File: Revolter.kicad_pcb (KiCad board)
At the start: 2 copper layers, 100 x 100 mm, 183 parts, among them IC1 LM5017, IC2 AP65111, IC3 INA181A1, IC4 INA181A1, J1 IO, P1 USB_OTG, P2 CAN, P3 IN+, P4 IN-, P5 MOTOR3, P6 MOTOR2, P7 MOTOR1, P8 SWD, P9 Motor, Q1 ZXTC2045E6, Q10 ZXTC2045E6, Q13 IRFB4110, Q14 IRFB4110, Q15 IRFB4110, Q16 IRFB4110, Q19 IRFB4110, Q2 ZXTC2045E6, Q20 IRFB4110, Q21 IRFB4110, Q22 IRFB4110, Q3 IRFB4110, Q4 IRFB4110, Q5 ZXTC2045E6, Q6 ZXTC2045E6, Q7 IRFB4110, Q8 IRFB4110, Q9 ZXTC2045E6, U1 STM32F40X_LQFP64, U2 IR2110S, U3 IR2110S, U4 IR2110S, U5 PCA82C251, U6 7805_SO8, Y1 Crystal

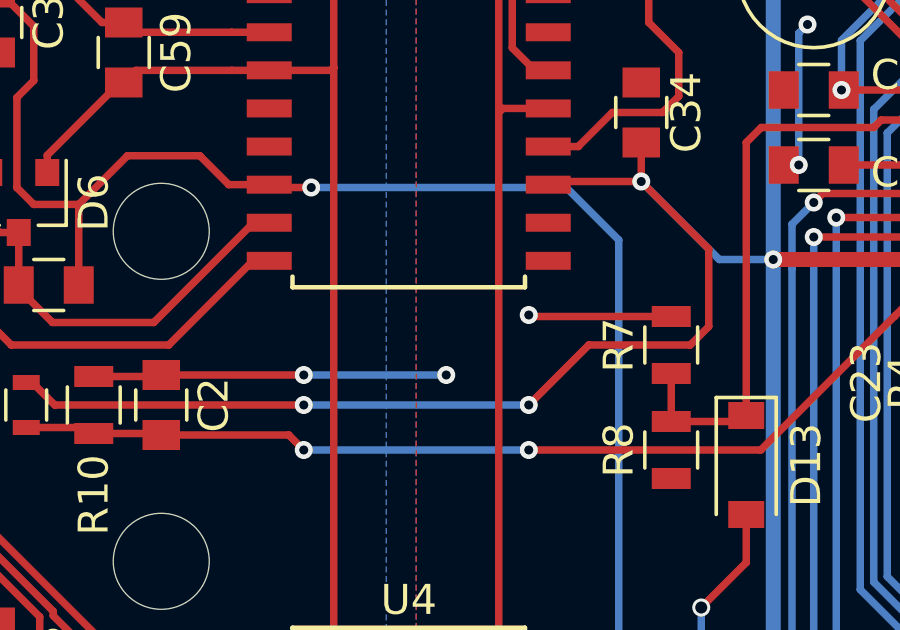
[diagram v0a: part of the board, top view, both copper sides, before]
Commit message: - fixed V_IN ADC channel missing a trace
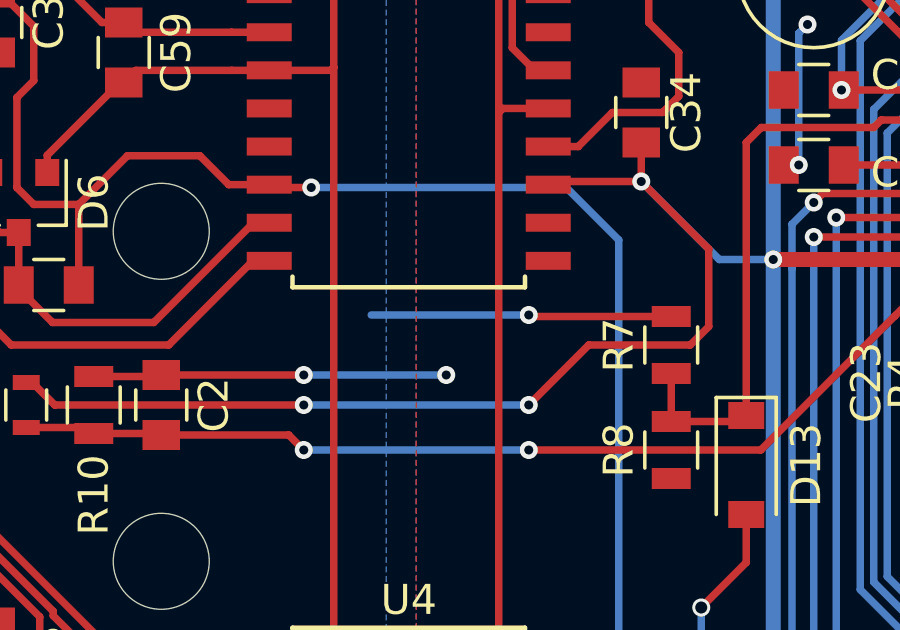
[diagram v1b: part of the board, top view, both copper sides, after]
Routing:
- net +BATT: track 46.9 -> 52.1 mm
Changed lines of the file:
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@@
     (thickness 1.6)
     (drawings 12)
-    (tracks 1598)
+    (tracks 1599)
     (zones 0)
     (modules 183)
@@
   (segment (start 110.525 132.7775) (end 110.2525 133.05) (width 0.5) (layer F.Cu) (net 32))
   (segment (start 110.2525 133.05) (end 108.75 133.05) (width 0.5) (layer F.Cu) (net 32))
+  (segment (start 118.25 66.25) (end 113 66.25) (width 0.25) (layer B.Cu) (net 32))
   (segment (start 134.25 69.45) (end 134.25 72.15) (width 0.25) (layer F.Cu) (net 33))
   (segment (start 137.35 72.15) (end 138.25 71.25) (width 0.25) (layer F.Cu) (net 34))

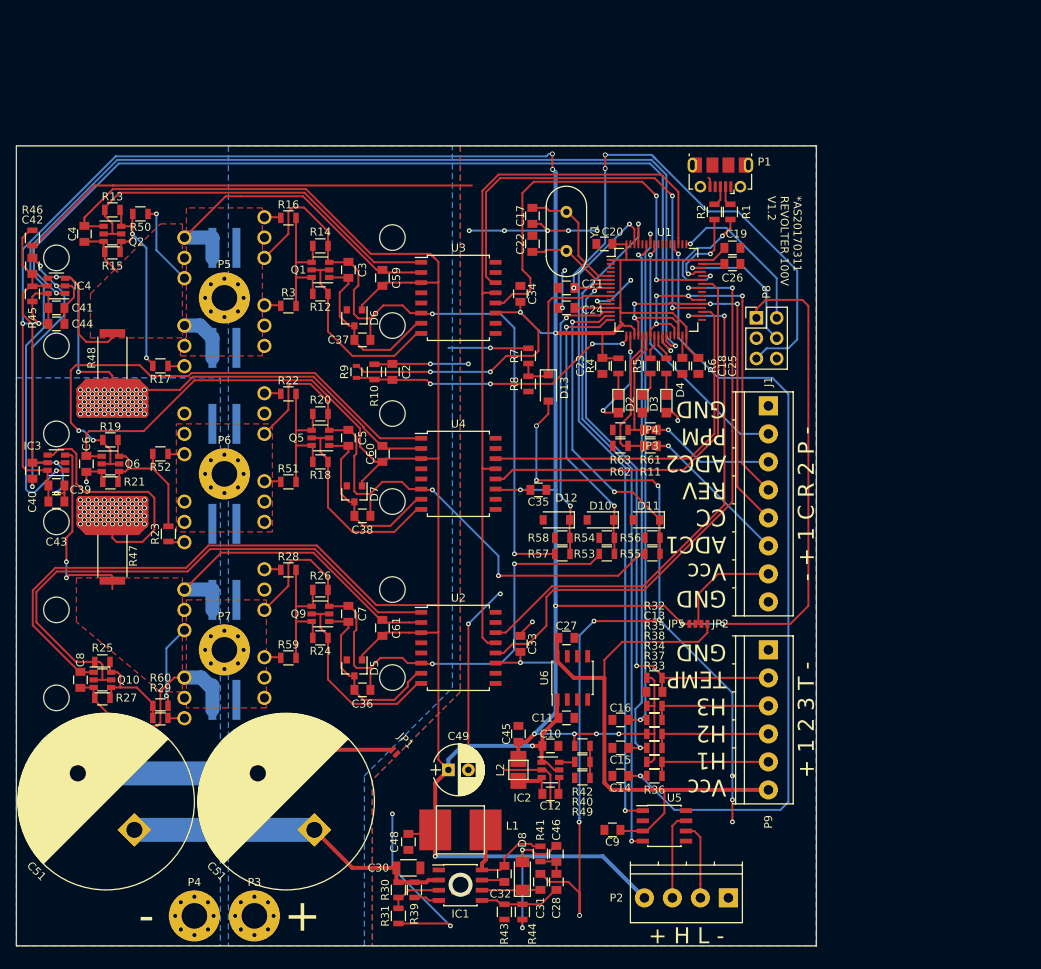
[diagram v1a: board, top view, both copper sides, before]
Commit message: - swapped TO220 dual MOSFET for single DualCool88 MOSFET package - removed postdriver - changed IRS2110 for IRS2186 - added third shunt - rewired CPU for VESC6 compatibility - layout completely from scratch
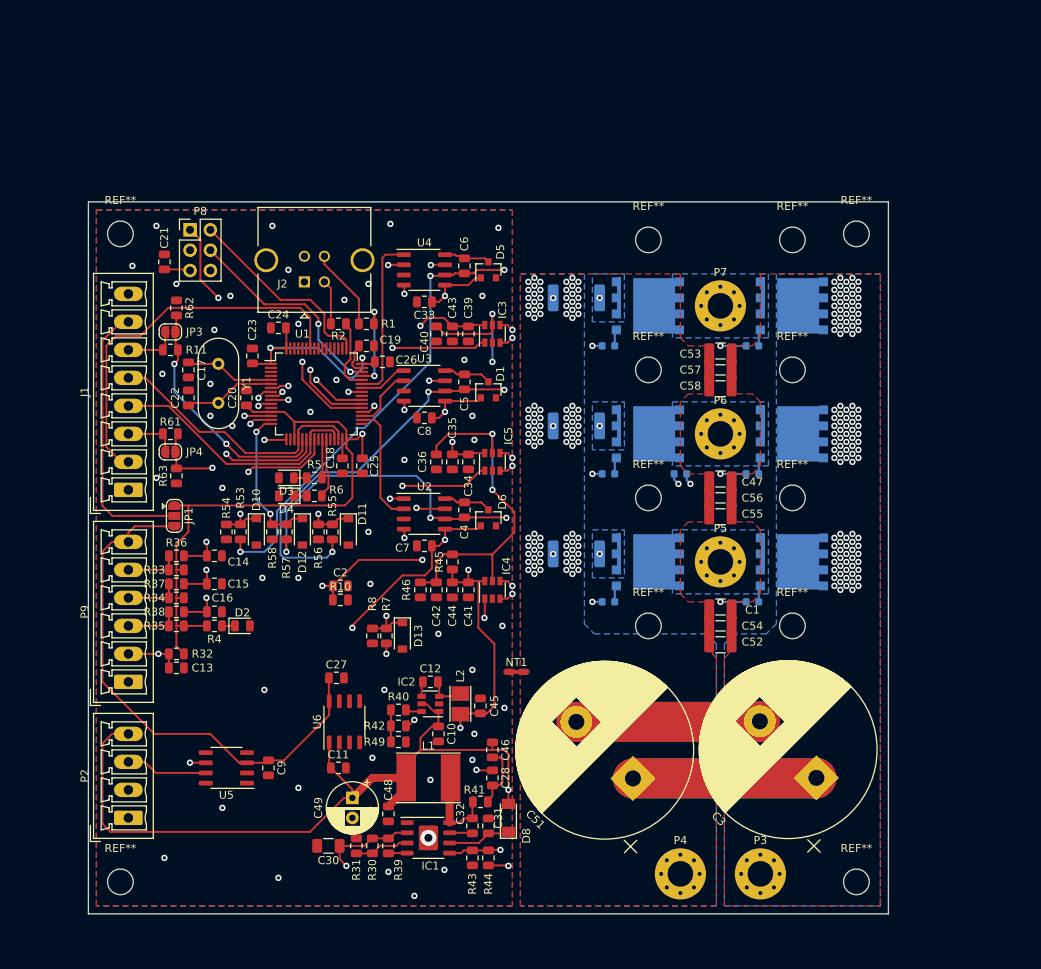
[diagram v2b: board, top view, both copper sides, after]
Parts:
- removed C29, C50, C62: 2u2 250V, Capacitors_SMD:C_1210
- removed C37, C38, C59, C60, C61: 100n, Capacitors_SMD:C_0805
- removed the C51 at (73.8, 126.5)
- removed the C51 at (96.2, 126.5)
- removed D7: BAS21L, Diodes_SMD:D_SOT-23_ANK
- removed JP2, JP5: opt., alexmod:Jumper_2
- removed P1: USB_OTG, Connectors_USB:USB_Micro-B_Molex-105017-0001
- removed Q10, Q9: ZXTC2045E6, TO_SOT_Packages_SMD:SOT-23-6
- removed Q13, Q14, Q15, Q16, Q19, Q20, Q21, Q22, Q7, Q8: IRFB4110, alexmod:TO220GDS_notab_rev
- removed R12, R13, R18, R19, R24, R25: 120R, Resistors_SMD:R_0805
- removed R14, R15, R20, R21, R26, R27: 10k, Resistors_SMD:R_0805
- removed R50, R51, R52, R59, R60: 1R, Resistors_SMD:R_0805
- added C51: 1mF 100V, Capacitor_THT:CP_Radial_D22.0mm_P10.00mm_SnapIn, F.Cu at (136.1, 120.1)
- added D1: BAS21L, Diode_SMD:D_SOT-23_ANK, F.Cu at (118.0, 71.5)
- added IC5: INA181A1, Package_TO_SOT_SMD:SOT-23-6, F.Cu at (118.5, 80.5)
- added J2: USB_A, Connector_USB:USB_B_TE_5787834_Vertical, F.Cu at (95.0, 58.0)
- added NT1: Net-Tie_2, NetTie:NetTie-2_SMD_Pad0.5mm, F.Cu at (121.5, 106.8)
- added REF**: MountingHole_3.2mm_M3, MountingHole:MountingHole_3.2mm_M3, F.Cu at (156.0, 52.8)
- added REF**: MountingHole_3.2mm_M3, MountingHole:MountingHole_3.2mm_M3, F.Cu at (138.0, 85.0)
- added REF**: MountingHole_3.2mm_M3, MountingHole:MountingHole_3.2mm_M3, F.Cu at (138.0, 69.0)
- added REF**: MountingHole_3.2mm_M3, MountingHole:MountingHole_3.2mm_M3, F.Cu at (138.0, 52.8)
- added REF**: MountingHole_3.2mm_M3, MountingHole:MountingHole_3.2mm_M3, F.Cu at (156.0, 69.0)
- added REF**: MountingHole_3.2mm_M3, MountingHole:MountingHole_3.2mm_M3, F.Cu at (156.0, 85.0)
- added REF**: MountingHole_3.2mm_M3, MountingHole:MountingHole_3.2mm_M3, F.Cu at (156.0, 101.0)
- added REF**: MountingHole_3.2mm_M3, MountingHole:MountingHole_3.2mm_M3, F.Cu at (164.0, 52.0)
- added REF**: MountingHole_3.2mm_M3, MountingHole:MountingHole_3.2mm_M3, F.Cu at (164.0, 133.0)
- added REF**: MountingHole_3.2mm_M3, MountingHole:MountingHole_3.2mm_M3, F.Cu at (72.0, 133.0)
- added REF**: MountingHole_3.2mm_M3, MountingHole:MountingHole_3.2mm_M3, F.Cu at (72.0, 52.0)
- added REF**: MountingHole_3.2mm_M3, MountingHole:MountingHole_3.2mm_M3, F.Cu at (138.0, 101.0)
- C1, C47, C52, C53, C54, C55, C56, C57, C58: footprint Capacitors_SMD:C_1210 -> Capacitor_SMD:C_1210_3225Metric; moved to F.Cu
- C10, C11, C12, C13, C14, C15, C16, C17, C18, C19, C2, C20, C21, C22, C23, C24, C25, C26, C27, C28, C31, C32, C36, C39, C4, C40, C41, C42, C43, C44, C45, C46, C48, C5, C6, C7, C8, C9: footprint Capacitors_SMD:C_0805 -> Capacitor_SMD:C_0805_2012Metric
- C3: value 1u -> 1mF 100V; footprint Capacitors_SMD:C_0805 -> Capacitor_THT:CP_Radial_D22.0mm_P10.00mm_SnapIn
- C30: footprint Capacitors_SMD:C_1206 -> Capacitor_SMD:C_1206_3216Metric
- C33, C35: value 100n -> 1u; footprint Capacitors_SMD:C_0805 -> Capacitor_SMD:C_0805_2012Metric
- C34: value 100n -> 10n; footprint Capacitors_SMD:C_0805 -> Capacitor_SMD:C_0805_2012Metric
- C49: footprint Capacitors_THT:CP_Radial_D6.3mm_P2.50mm -> Capacitor_THT:CP_Radial_D6.3mm_P2.50mm
- D10, D11, D12, D13: footprint Diodes_SMD:D_SOD-123 -> Diode_SMD:D_SOD-123
- D2, D3, D4: footprint LEDs:LED_0805 -> LED_SMD:LED_0805_2012Metric
- D5, D6: footprint Diodes_SMD:D_SOT-23_ANK -> Diode_SMD:D_SOT-23_ANK
- D8: footprint Diodes_SMD:D_MiniMELF_Standard -> Diode_SMD:D_MiniMELF
- IC1: footprint Housings_SOIC:SOIC-8-1EP_3.9x4.9mm_Pitch1.27mm -> Package_SO:HSOP-8-1EP_3.9x4.9mm_P1.27mm_EP2.41x3.1mm
- IC2, IC3, IC4: footprint TO_SOT_Packages_SMD:SOT-23-6 -> Package_TO_SOT_SMD:SOT-23-6
- J1: footprint Connectors_Terminal_Blocks:TerminalBlock_Pheonix_PT-3.5mm_8pol -> Connector_Phoenix_MC:PhoenixContact_MCV_1,5_8-G-3.5_1x08_P3.50mm_Vertical
- JP1: value JUMPER -> Jumper_NC_Dual; footprint alexmod:Jumper_2 -> Jumper:SolderJumper-3_P1.3mm_Open_RoundedPad1.0x1.5mm
- JP3, JP4: footprint alexmod:Jumper_2 -> Jumper:SolderJumper-2_P1.3mm_Open_RoundedPad1.0x1.5mm
- L1: footprint alexmod:VLS6045EX -> Inductor_SMD:L_Taiyo-Yuden_NR-60xx_HandSoldering
- L2: footprint alexmod:NRH2410 -> Inductor_SMD:L_Taiyo-Yuden_NR-24xx_HandSoldering
- P2: footprint Connectors_Terminal_Blocks:TerminalBlock_Pheonix_PT-3.5mm_4pol -> Connector_Phoenix_MC:PhoenixContact_MCV_1,5_4-G-3.5_1x04_P3.50mm_Vertical
- P3, P4, P5, P6, P7: footprint Mounting_Holes:MountingHole_3.2mm_M3_Pad_Via -> MountingHole:MountingHole_3.2mm_M3_Pad_Via
- P8: footprint Pin_Headers:Pin_Header_Straight_2x03_Pitch2.54mm -> Connector_PinHeader_2.54mm:PinHeader_2x03_P2.54mm_Vertical
- P9: footprint Connectors_Terminal_Blocks:TerminalBlock_Pheonix_PT-3.5mm_6pol -> Connector_Phoenix_MC:PhoenixContact_MCV_1,5_6-G-3.5_1x06_P3.50mm_Vertical
- Q1, Q2, Q5, Q6: value ZXTC2045E6 -> FDMT800100DC; footprint TO_SOT_Packages_SMD:SOT-23-6 -> Package_TO_SOT_SMD:PQFN_8x8; moved to B.Cu
- Q3, Q4: value IRFB4110 -> FDMT800100DC; footprint alexmod:TO220GDS_notab_rev -> Package_TO_SOT_SMD:PQFN_8x8
- R1, R10, R11, R2, R30, R31, R32, R33, R34, R35, R36, R37, R38, R39, R4, R40, R41, R42, R43, R44, R45, R46, R49, R5, R53, R54, R55, R56, R57, R58, R6, R61, R62, R63, R7, R8: footprint Resistors_SMD:R_0805 -> Resistor_SMD:R_0805_2012Metric
- R16, R17, R22, R23, R28, R29: footprint Resistors_SMD:R_0805 -> Resistor_SMD:R_0603_1608Metric; moved to B.Cu
- R3: value 1R -> WSLF2512L5000FEB; footprint Resistors_SMD:R_0805 -> Resistor_SMD:R_2512_6332Metric; moved to B.Cu
- R47, R48: footprint Resistors_SMD:R_2512 -> Resistor_SMD:R_2512_6332Metric; moved to B.Cu
- R9: footprint Resistors_SMD:R_0603 -> Resistor_SMD:R_0603_1608Metric; moved to B.Cu
- U1: footprint Housings_QFP:LQFP-64_10x10mm_Pitch0.5mm -> Package_QFP:LQFP-64_10x10mm_P0.5mm
- U2, U3, U4: value IR2110S -> IRS2186; footprint Housings_SOIC:SOIC-16W_7.5x10.3mm_Pitch1.27mm -> Package_SO:SO-8_3.9x4.9mm_P1.27mm
- U5, U6: footprint Housings_SOIC:SOIC-8_3.9x4.9mm_Pitch1.27mm -> Package_SO:SO-8_3.9x4.9mm_P1.27mm
- Y1: footprint Crystals:Crystal_HC49-U_Vertical -> Crystal:Crystal_HC49-U_Vertical
- moved C3 86.3 mm to (159.0, 120.0), turned to 135 degrees
- moved J1 80.7 mm to (73.0, 84.0), turned to 90 degrees
- moved P9 80.1 mm to (73.0, 108.0), turned to 90 degrees
- moved C54 78.7 mm to (147.0, 101.0)
- moved Q2 78.5 mm to (137.9, 93.0)
- moved P2 75.7 mm to (73.0, 125.0), turned to 90 degrees
- moved P7 75.5 mm to (147.0, 61.0)
- moved R16 75.3 mm to (151.0, 98.0), turned to 180 degrees
- moved C58 74.1 mm to (147.0, 71.0)
- moved R29 72.8 mm to (133.0, 66.0)
- moved P8 71.6 mm to (80.7, 51.5)
- moved C52 71.4 mm to (147.0, 103.0)
- moved C1 70.7 mm to (147.0, 99.0)
- moved Q3 70.4 mm to (155.9, 77.0)
- moved P5 70.2 mm to (147.0, 93.0)
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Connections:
- net /MCU/DC_CAL renamed Net-(U1-Pad33)
- net /MCU/FAULT renamed Net-(U1-Pad53)
- net /MCU/SENS2 renamed /MCU/VOLTAGE_2
- C1 pad 2: /Mosfet driver/H1_LOW -> GNDPWR
- C3 pad 1: /Mosfet driver/H1_HI -> +BATT
- C3 pad 2: /Mosfet driver/H1_VS -> GNDPWR
- C33 pad 1: GND -> +12V
- C33 pad 2: +3V3 -> GND
- C34 pad 1: GND -> +3V3
- C34 pad 2: +3V3 -> GND
- C35 pad 1: GND -> +3V3
- C35 pad 2: +3V3 -> GND
- C36 pad 1: /Mosfet driver/H3_HI -> U/2
- C36 pad 2: /Mosfet driver/H3_VS -> GND
- C4 pad 1: +12V -> Net-(C4-Pad1)
- C4 pad 2: /Mosfet driver/H1_LOW -> /Mosfet driver/H1_VS
- C5 pad 1: /Mosfet driver/H2_HI -> Net-(C5-Pad1)
- C52 pad 2: /Mosfet driver/H1_LOW -> GNDPWR
- C53 pad 2: /Mosfet driver/H3_LOW -> GNDPWR
- C54 pad 2: /Mosfet driver/H1_LOW -> GNDPWR
- C57 pad 2: /Mosfet driver/H3_LOW -> GNDPWR
- C58 pad 2: /Mosfet driver/H3_LOW -> GNDPWR
- C6 pad 1: +12V -> Net-(C6-Pad1)
- C6 pad 2: GNDPWR -> /Mosfet driver/H3_VS
- C7 pad 1: /Mosfet driver/H3_HI -> +12V
- C7 pad 2: /Mosfet driver/H3_VS -> GND
- C8 pad 2: /Mosfet driver/H3_LOW -> GND
- D10 pad 1: /MCU/SENS1 -> /MCU/VOLTAGE_1
- D12 pad 1: /MCU/SENS3 -> /MCU/VOLTAGE_3
- D5 pad 1: /Mosfet driver/H3_HI -> Net-(C6-Pad1)
- D6 pad 1: /Mosfet driver/H1_HI -> Net-(C4-Pad1)
- IC3 pad 1: /MCU/BR_SO1 -> /MCU/CURRENT_3
- IC4 pad 1: /MCU/BR_SO2 -> /MCU/CURRENT_1
- J1 pad 4: /MCU/RX_SCL_MOSI -> /MCU/TX_SCL_MOSI
- J1 pad 5: /MCU/TX_SDA_NSS -> /MCU/RX_SDA_NSS
- JP1 pad 1: GND -> +3V3
- JP1 pad 2: GNDPWR -> Net-(J1-Pad7)
- Q1 pad 1: /Mosfet driver/H1_HI -> Net-(Q1-Pad1)
- Q1 pad 2: /Mosfet driver/M_H1 -> /Mosfet driver/H1_VS
- Q1 pad 3: /Mosfet driver/H1_VS -> +BATT
- Q2 pad 1: +12V -> Net-(Q2-Pad1)
- Q2 pad 2: /Mosfet driver/M_L1 -> /Mosfet driver/H1_LOW
- Q2 pad 3: /Mosfet driver/H1_LOW -> /Mosfet driver/H1_VS
- Q3 pad 2: +BATT -> /Mosfet driver/H2_VS
- Q3 pad 3: /Mosfet driver/H1_VS -> +BATT
- Q4 pad 2: /Mosfet driver/H1_VS -> /Mosfet driver/H2_LOW
- Q4 pad 3: /Mosfet driver/H1_LOW -> /Mosfet driver/H2_VS
- Q5 pad 1: /Mosfet driver/H2_HI -> Net-(Q5-Pad1)
- Q5 pad 2: /Mosfet driver/M_H2 -> /Mosfet driver/H3_VS
- Q5 pad 3: /Mosfet driver/H2_VS -> +BATT
- Q6 pad 1: +12V -> Net-(Q6-Pad1)
- Q6 pad 2: /Mosfet driver/M_L2 -> /Mosfet driver/H3_LOW
- Q6 pad 3: GNDPWR -> /Mosfet driver/H3_VS
- R1 pad 1: /MCU/USB_DM -> /MCU/USB_DP
- R16 pad 1: Net-(Q3-Pad1) -> Net-(Q1-Pad1)
- R16 pad 2: Net-(Q1-Pad4) -> /Mosfet driver/M_H1
- R17 pad 1: Net-(Q4-Pad1) -> Net-(Q2-Pad1)
- R17 pad 2: Net-(Q2-Pad4) -> /Mosfet driver/M_L1
- R2 pad 1: /MCU/USB_DP -> /MCU/USB_DM
- R22 pad 1: Net-(Q13-Pad1) -> Net-(Q3-Pad1)
- R22 pad 2: Net-(Q5-Pad4) -> /Mosfet driver/M_H2
- R23 pad 1: Net-(Q14-Pad1) -> Net-(Q4-Pad1)
- R23 pad 2: Net-(Q6-Pad4) -> /Mosfet driver/M_L2
- R28 pad 1: Net-(Q19-Pad1) -> Net-(Q5-Pad1)
- R28 pad 2: Net-(Q9-Pad4) -> /Mosfet driver/M_H3
- R29 pad 1: Net-(Q20-Pad1) -> Net-(Q6-Pad1)
- R29 pad 2: Net-(Q10-Pad4) -> /Mosfet driver/M_L3
- R3 pad 1: Net-(Q7-Pad1) -> GNDPWR
- R3 pad 2: Net-(Q1-Pad4) -> /Mosfet driver/H2_LOW
- R53 pad 2: /MCU/SENS1 -> /MCU/VOLTAGE_1
- R54 pad 2: /MCU/SENS1 -> /MCU/VOLTAGE_1
- R57 pad 2: /MCU/SENS3 -> /MCU/VOLTAGE_3
- R58 pad 2: /MCU/SENS3 -> /MCU/VOLTAGE_3
- U1 pad 10: /MCU/AN_IN -> /MCU/CURRENT_3
- U1 pad 11: Net-(U1-Pad11) -> /MCU/AN_IN
- U1 pad 14: /MCU/SENS3 -> /MCU/VOLTAGE_1
- U1 pad 16: /MCU/SENS1 -> /MCU/VOLTAGE_3
- U1 pad 20: /MCU/TX_SDA_NSS -> /MCU/RX_SDA_NSS
- U1 pad 23: /MCU/RX_SCL_MOSI -> /MCU/TX_SCL_MOSI
- U1 pad 24: /MCU/LED_GREEN -> /Filters/TEMP_IN
- U1 pad 25: /MCU/LED_RED -> Net-(U1-Pad25)
- U1 pad 26: /MCU/BR_SO2 -> /MCU/LED_GREEN
- U1 pad 27: /MCU/BR_SO1 -> /MCU/LED_RED
- U1 pad 29: /MCU/RX_SCL_MOSI -> /MCU/TX_SCL_MOSI
- U1 pad 30: /MCU/TX_SDA_NSS -> /MCU/RX_SDA_NSS
- U1 pad 34: /MCU/L3 -> /MCU/L1
- U1 pad 36: /MCU/L1 -> /MCU/L3
- U1 pad 37: /MCU/TX_SDA_NSS -> /Filters/HALL1_OUT
- U1 pad 38: /MCU/RX_SCL_MOSI -> /Filters/HALL2_OUT
- U1 pad 39: Net-(U1-Pad39) -> /Filters/HALL3_OUT
- U1 pad 41: /MCU/H3 -> /MCU/H1
- U1 pad 43: /MCU/H1 -> /MCU/H3
- U1 pad 51: /MCU/EN_GATE -> Net-(U1-Pad51)
- U1 pad 52: /Filters/HALL3_OUT -> Net-(U1-Pad52)
- U1 pad 57: /MCU/SERVO -> Net-(U1-Pad57)
- U1 pad 58: /Filters/HALL1_OUT -> /MCU/SERVO
- U1 pad 59: /Filters/HALL2_OUT -> Net-(U1-Pad59)
- U1 pad 8: /Filters/TEMP_IN -> /MCU/CURRENT_1
- U1 pad 9: Net-(U1-Pad9) -> /MCU/CURRENT_2
- U2 pad 1: /Mosfet driver/M_L3 -> /MCU/H1
- U2 pad 2: /Mosfet driver/H3_LOW -> /MCU/L1
- U2 pad 3: +12V -> GND
- U2 pad 4: (no net) -> /Mosfet driver/M_L1
- U2 pad 5: (no net) -> +12V
- U2 pad 6: /Mosfet driver/H3_VS -> /Mosfet driver/H1_VS
- U2 pad 7: /Mosfet driver/H3_HI -> /Mosfet driver/M_H1
- U2 pad 8: /Mosfet driver/M_H3 -> Net-(C4-Pad1)
- U3 pad 1: /Mosfet driver/M_L1 -> /MCU/H2
- U3 pad 2: /Mosfet driver/H1_LOW -> /MCU/L2
- U3 pad 3: +12V -> GND
- U3 pad 4: (no net) -> /Mosfet driver/M_L2
- U3 pad 5: (no net) -> +12V
- U3 pad 6: /Mosfet driver/H1_VS -> /Mosfet driver/H2_VS
- U3 pad 7: /Mosfet driver/H1_HI -> /Mosfet driver/M_H2
- U3 pad 8: /Mosfet driver/M_H1 -> Net-(C5-Pad1)
- U4 pad 1: /Mosfet driver/M_L2 -> /MCU/H3
- U4 pad 2: GNDPWR -> /MCU/L3
- U4 pad 3: +12V -> GND
- U4 pad 4: (no net) -> /Mosfet driver/M_L3
- U4 pad 5: (no net) -> +12V
- U4 pad 6: /Mosfet driver/H2_VS -> /Mosfet driver/H3_VS
- U4 pad 7: /Mosfet driver/H2_HI -> /Mosfet driver/M_H3
- U4 pad 8: /Mosfet driver/M_H2 -> Net-(C6-Pad1)
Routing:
- net GND: track 356.3 -> 0.75 mm, vias 35 -> 48
- net GNDPWR: track 345.1 -> 77.4 mm, vias 123 -> 102
- net /MCU/BR_SO1: track 146.9 -> 0.00 mm, vias 2 -> 0
- net +3V3: track 427.3 -> 300.7 mm, vias 17 -> 10
- net +12V: track 358.0 -> 232.5 mm, vias 4 -> 6
- net /MCU/BR_SO2: track 116.1 -> 0.00 mm, vias 2 -> 0
- net (no net): track 100.0 -> 0.00 mm
- net /MCU/EN_GATE: track 94.0 -> 0.00 mm
- net +BATT: track 52.1 -> 144.8 mm, vias 1 -> 113
- net /CAN bus transceiver/CAN_RX: track 86.5 -> 0.00 mm, vias 2 -> 0
- net /CAN bus transceiver/CAN_TX: track 83.3 -> 0.00 mm, vias 2 -> 0
- net /Mosfet driver/H3_LOW: track 93.0 -> 16.6 mm
- net /Filters/HALL3_OUT: track 102.5 -> 40.8 mm
- net /MCU/TX_SDA_NSS: track 52.8 -> 0.00 mm, vias 4 -> 0
- net /MCU/H3: track 73.5 -> 20.9 mm, vias 2 -> 0
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- added copper zone on F.Cu, net +BATT
- added copper zone on B.Cu, net /Mosfet driver/H1_LOW
- added copper zone on B.Cu, net /Mosfet driver/H1_VS
- added copper zone on B.Cu, net /Mosfet driver/H2_LOW
- added copper zone on B.Cu, net /Mosfet driver/H2_VS
- added copper zone on B.Cu, net /Mosfet driver/H3_LOW
- added copper zone on B.Cu, net /Mosfet driver/H3_VS
- added copper zone on F.Cu, net GNDPWR
- removed copper zone on F.Cu, net /Mosfet driver/H1_LOW
- removed copper zone on F.Cu, net /Mosfet driver/H1_VS
- removed copper zone on F.Cu, net /Mosfet driver/H2_VS
- removed copper zone on F.Cu, net /Mosfet driver/H3_LOW
- removed copper zone on F.Cu, net /Mosfet driver/H3_VS
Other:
- board size 100 x 100 mm -> 100 x 89 mm
- copper layers 2 -> 4
- net class Default: via_dia 0.6 -> 0.8; via_drill 0.3 -> 0.4
- rule pad_to_mask_clearance: 0.1 -> 0
- rule via_min_size: 0.6 -> 0.4
- board text removed: "*AS20170311 REVOLTER 100V V1.2"
- board text removed: "+"
- board text removed: "+ 1 2 3 T -"
- board text removed: "+ H L -"
- board text removed: "-"
- board text removed: "- + 1 C R 2 P -"
- board text removed: "GND Vcc ADC1 CC REV ADC2 PPM GND"
- board text removed: "Vcc H1 H2 H3 TEMP GND"

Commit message: - added some planes - cleaned some traces - added labels for the connectors
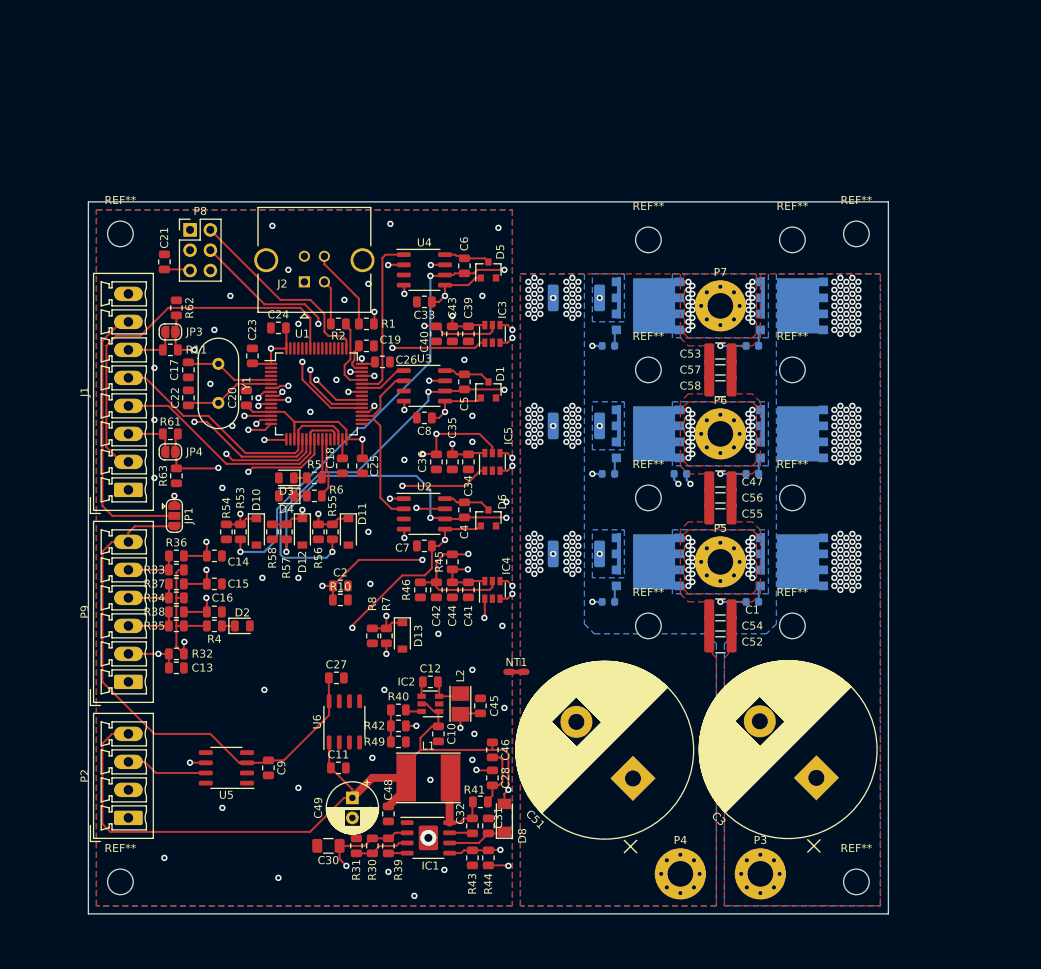
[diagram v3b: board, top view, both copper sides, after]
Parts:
- moved D8 0.50 mm to (120.0, 125.0)
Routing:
- net +3V3: track 300.7 -> 103.7 mm, vias 10 -> 12
- net +BATT: track 144.8 -> 98.9 mm
- net GNDPWR: track 77.4 -> 31.5 mm
- net /Mosfet driver/H1_VS: track 69.3 -> 65.3 mm, vias 3 -> 27
- net /MCU/VOLTAGE_3: track 18.7 -> 21.6 mm
- net U/2: track 68.4 -> 70.9 mm
- net /MCU/SCK_ADC_EXT: track 31.0 -> 32.6 mm
- net /MCU/VOLTAGE_2: track 22.9 -> 21.8 mm
- net /MCU/CURRENT_3: track 30.6 -> 31.2 mm
- net /Mosfet driver/M_H2: track 58.0 -> 57.4 mm
- net /Mosfet driver/H3_VS: track 86.7 -> 86.5 mm, vias 3 -> 27
- net GND: vias 48 -> 45
- net /Mosfet driver/H2_VS: vias 3 -> 27
- added copper zone on Power, net +3V3
- added copper zone on F.Cu, net /Mosfet driver/H1_VS
- added copper zone on Power, net /Mosfet driver/H1_VS
- added copper zone on Sig, net /Mosfet driver/H1_VS
- added copper zone on F.Cu, net /Mosfet driver/H2_VS
- added copper zone on Power, net /Mosfet driver/H2_VS
- added copper zone on Sig, net /Mosfet driver/H2_VS
- added copper zone on F.Cu, net /Mosfet driver/H3_VS
- added copper zone on Power, net /Mosfet driver/H3_VS
- added copper zone on Sig, net /Mosfet driver/H3_VS
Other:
- board text added: "+ H L -"
- board text added: "+ H3 H2 H1 T -"
- board text added: "- + A1 CC REV A2 PPM -"

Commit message: - added a via for some plane fills - removed silkscreen labels that don't make sense - widened plane spokes width to 1mm - minor tweaks - added version text - changed plotter settings to use home point - base for V1.2
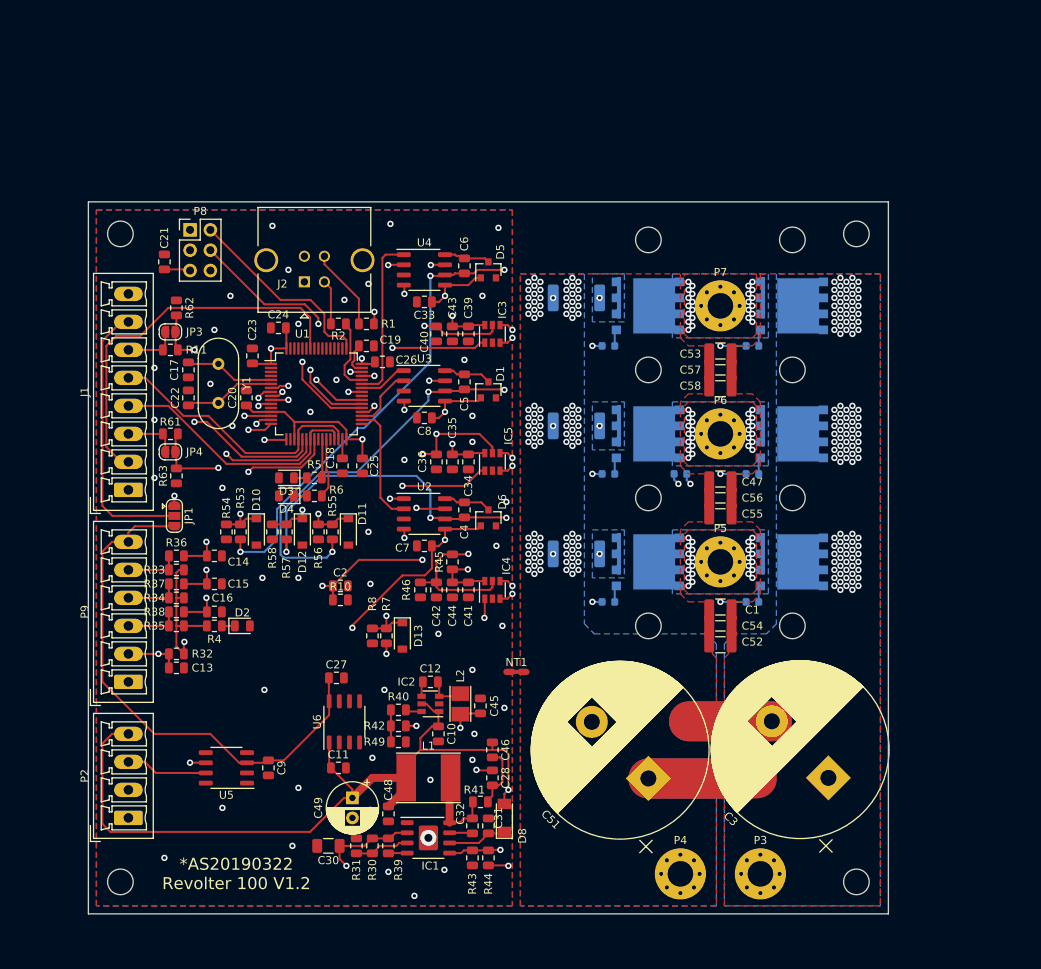
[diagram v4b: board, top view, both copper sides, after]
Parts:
- moved C51 1.93 mm to (138.0, 120.1)
- moved C3 1.50 mm to (160.5, 120.0)
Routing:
- net +BATT: track 98.9 -> 128.2 mm
- net GNDPWR: track 31.5 -> 52.2 mm
- net GND: vias 45 -> 46
- added copper zone on Power, net +BATT
- added copper zone on Power, net GNDPWR
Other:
- rule pad_to_mask_clearance: 0 -> 0.1
- board text added: "*AS20190322 Revolter 100 V1.2"
